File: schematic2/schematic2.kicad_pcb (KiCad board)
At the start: 2 copper layers, 68.8 x 56 mm, 52 parts, among them IC1 CAT24C32WI-GT3, J1 Barrel_Jack, K1 TIANBO_HJR_1-2C, P1 Conn_02x20_Odd_Even, Q1 BC547, Q2 BC557, Q3 BC547, Q4 BC547, U1 buck, U2 DS3231M, U3 MCP1700-1202E_SOT89

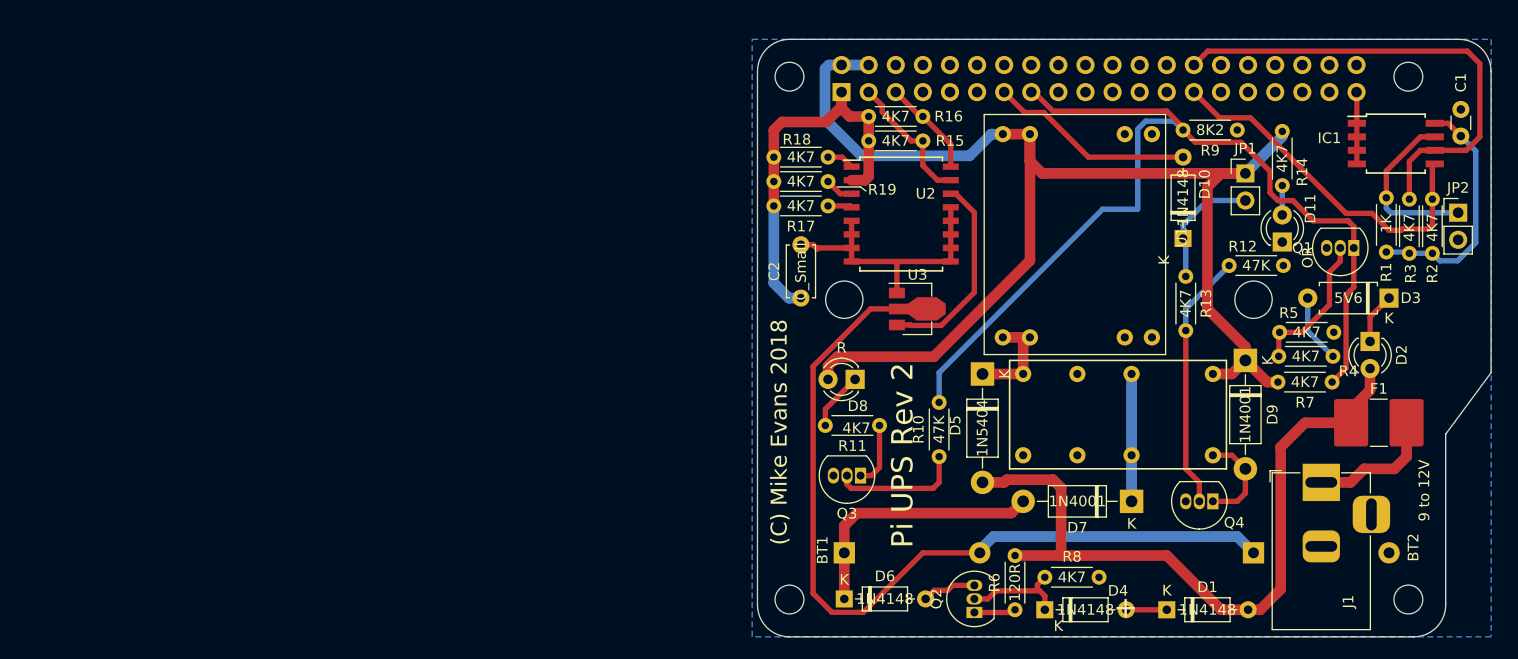
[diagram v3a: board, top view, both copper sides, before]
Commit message: Power the 3V line instead of the 5V.
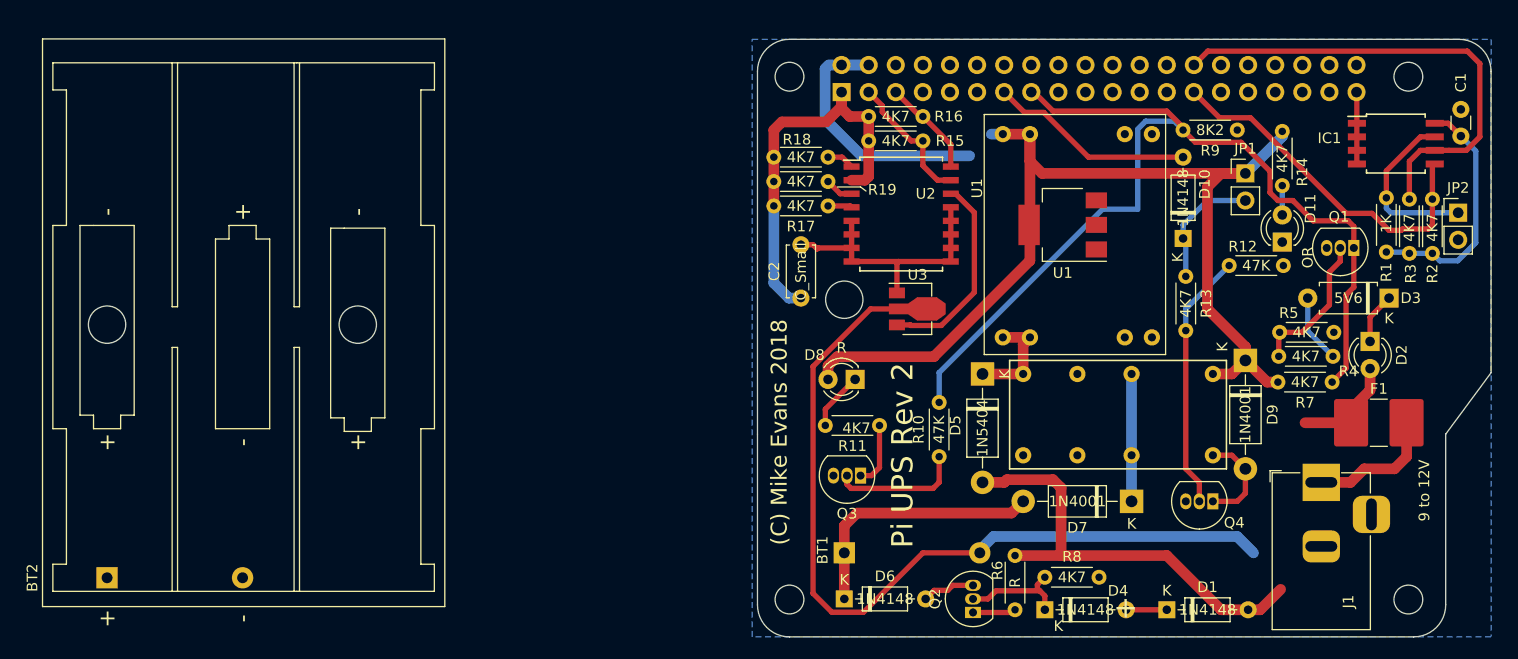
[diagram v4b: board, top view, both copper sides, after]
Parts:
- added U1: AP1117-33, Package_TO_SOT_SMD:SOT-223-3_TabPin2, F.Cu at (229.1, 111.4)
- BT2: value 3x AAA NiMh -> 4x AAA NiMh
- Q2: value BC557 -> 2N2907
- R6: value 120R -> R
- moved BT2 107.5 mm to (139.5, 144.5)
- moved Q2 0.13 mm to (220.7, 147.7)
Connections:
- BT1 pad 1: Net-(BT1-Pad1) -> (no net)
- D1 pad 2: +9V -> +5V
- D2 pad 2: +9V -> +5V
- D5 pad 1: Net-(D5-Pad1) -> Net-(C3-Pad1)
- D5 pad 2: +9V -> +5V
- D6 pad 1: Net-(BT1-Pad1) -> /Sheet5B4BA297/VI
- D7 pad 2: Net-(BT1-Pad1) -> /Sheet5B4BA297/VI
- D8 pad 2: +5V -> +3V3
- D9 pad 1: +5V -> Net-(C3-Pad1)
- F1 pad 1: +9V -> (no net)
- JP1 pad 1: +5V -> +3V3
- JP2 pad 2: Net-(JP2-Pad2) -> (no net)
- K1 pad 11: Net-(K1-Pad11) -> (no net)
- K1 pad 16: +5V -> Net-(C3-Pad1)
- K1 pad 6: Net-(K1-Pad6) -> (no net)
- K1 pad 8: Net-(K1-Pad8) -> (no net)
- K1 pad 9: Net-(D5-Pad1) -> Net-(C3-Pad1)
- P1 pad 10: /GPIO15(RXD0) -> (no net)
- P1 pad 11: /GPIO17(GEN0) -> (no net)
- P1 pad 12: /GPIO18(GEN1)(PWM0) -> (no net)
- P1 pad 16: /GPIO23(GEN4) -> (no net)
- P1 pad 17: Net-(P1-Pad17) -> (no net)
- P1 pad 18: /GPIO24(GEN5) -> (no net)
- P1 pad 19: /GPIO10(SPI0_MOSI) -> (no net)
- P1 pad 21: /GPIO9(SPI0_MISO) -> (no net)
- P1 pad 22: /GPIO25(GEN6) -> (no net)
- P1 pad 23: /GPIO11(SPI0_SCK) -> (no net)
- P1 pad 24: /GPIO8(SPI0_CE_N) -> (no net)
- P1 pad 26: /GPIO7(SPI1_CE_N) -> (no net)
- P1 pad 29: /GPIO5 -> (no net)
- P1 pad 3: SDA1 -> SCL1
- P1 pad 31: /GPIO6 -> (no net)
- P1 pad 32: /GPIO12(PWM0) -> (no net)
- P1 pad 33: /GPIO13(PWM1) -> (no net)
- P1 pad 35: /GPIO19(SPI1_MISO) -> (no net)
- P1 pad 36: /GPIO16 -> (no net)
- P1 pad 37: /GPIO26 -> (no net)
- P1 pad 38: /GPIO20(SPI1_MOSI) -> (no net)
- P1 pad 40: /GPIO21(SPI1_SCK) -> (no net)
- P1 pad 7: /GPIO4(GCLK) -> (no net)
- P1 pad 8: /GPIO14(TXD0) -> (no net)
- R14 pad 2: +5V -> +3V3
- R15 pad 1: SDA1 -> SCL1
- R2 pad 1: Net-(R2-Pad1) -> (no net)
- R3 pad 1: Net-(R3-Pad1) -> (no net)
- R6 pad 2: +9V -> +5V
- R7 pad 2: +5V -> +3V3
- U1 pad 4: +5V -> +3V3
- U2 pad 15: SDA1 -> SCL1
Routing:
- net +3V3: track 37.9 -> 134.9 mm
- net +9V: track 68.6 -> 0.00 mm
- net +5V: track 123.9 -> 76.0 mm
- net Net-(BT1-Pad1): track 24.6 -> 0.00 mm
- net /Sheet5B4BA297/VI: track 81.2 -> 105.8 mm
- net SDA1: track 12.9 -> 0.00 mm
- net SCL1: track 9.33 -> 22.2 mm

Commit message: Re-layout.
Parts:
- removed BT1: 3x AAA NiMh, Battery:BatteryHolder_Keystone_2479_3xAAA
- removed F1: Polyfuse, Fuse:Fuse_2816_7142Metric_Pad3.20x4.45mm_HandSolder
- removed IC1: CAT24C32WI-GT3, Package_SO:SOIJ-8_5.3x5.3mm_P1.27mm
- removed J1: Barrel_Jack, Connector_BarrelJack:BarrelJack_Horizontal
- removed MK1, MK2, MK3, MK4: M2.5, MountingHole:MountingHole_2.7mm_M2.5
- removed R3: 4K7, Resistor_THT:R_Axial_DIN0204_L3.6mm_D1.6mm_P5.08mm_Horizontal
- removed U3: MCP1700-1202E_SOT89, Package_TO_SOT_SMD:SOT-89-3
- added C3: 10uF, Capacitor_THT:CP_Radial_D6.3mm_P2.50mm, F.Cu at (214.7, 133.0)
- added C4: 22uF, Capacitor_THT:CP_Radial_D6.3mm_P2.50mm, F.Cu at (214.7, 125.4)
- added REF**: MountingHole_2.7mm_M2.5_Pad, MountingHole:MountingHole_2.7mm_M2.5_Pad, F.Cu at (203.4, 146.6)
- added REF**: MountingHole_2.7mm_M2.5_Pad, MountingHole:MountingHole_2.7mm_M2.5_Pad, F.Cu at (261.4, 146.6)
- added U4: CAT24C256, Package_SO:SOIC-8_3.9x4.9mm_P1.27mm, F.Cu at (261.0, 103.5)
- BT2: footprint Battery:BatteryHolder_Keystone_2479_3xAAA -> Connector_Molex:Molex_KK-254_AE-6410-02A_1x02_P2.54mm_Vertical
- C1: value 0.1uF -> C_Small
- C2: value C_Small -> 100nF
- R1: value 1K -> 4K7
- moved BT2 71.3 mm to (210.7, 139.8), turned to 180 degrees
- moved R11 43.6 mm to (254.9, 137.8), turned to 90 degrees
- moved D8 42.7 mm to (251.8, 132.5)
- moved Q3 40.2 mm to (250.3, 136.5), turned to 270 degrees
- moved R10 39.9 mm to (257.1, 137.8)
- moved R18 5.84 mm to (207.1, 110.9)
- moved R19 5.59 mm to (207.1, 112.9)
- moved U2 5.36 mm to (214.5, 115.7)
- moved R17 5.33 mm to (207.1, 114.9)
- moved R15 4.85 mm to (216.5, 108.3)
- moved R16 4.58 mm to (216.3, 105.8)
- moved R1 3.81 mm to (255.6, 108.9), turned to 90 degrees
- moved C2 2.34 mm to (202.8, 119.8), turned to 0 degrees
- moved U1 1.90 mm to (231.0, 111.1), turned to 90 degrees
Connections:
- BT2 pad 1: /Sheet5B4BA297/VI -> Net-(BT2-Pad1)
- C1 pad 1: +3.3V -> +3V3
- C2 pad 1: +3V3 -> /Sheet5B4BA297/VI
- D6 pad 1: /Sheet5B4BA297/VI -> Net-(BT2-Pad1)
- D7 pad 2: /Sheet5B4BA297/VI -> Net-(BT2-Pad1)
- D9 pad 2: Net-(D9-Pad2) -> /Sheet5B4BA297/VI
- JP2 pad 2: (no net) -> GND
- K1 pad 1: Net-(D9-Pad2) -> /Sheet5B4BA297/VI
- P1 pad 3: SCL1 -> SDA1
- Q4 pad 1: Net-(D9-Pad2) -> /Sheet5B4BA297/VI
- R1 pad 1: Net-(IC1-Pad7) -> +3V3
- R1 pad 2: +3.3V -> ID_SD
- R15 pad 2: +3V3 -> /Sheet5B4BA297/VI
- R16 pad 1: SCL1 -> SDA1
- R16 pad 2: +3V3 -> /Sheet5B4BA297/VI
- R17 pad 2: +3V3 -> /Sheet5B4BA297/VI
- R18 pad 2: +3V3 -> /Sheet5B4BA297/VI
- R19 pad 2: +3V3 -> /Sheet5B4BA297/VI
- R2 pad 1: (no net) -> +3V3
- R2 pad 2: ID_SD -> ID_SC
- U2 pad 14: Net-(U2-Pad14) -> (no net)
- U2 pad 15: SCL1 -> SDA1
- U2 pad 2: +3V3 -> /Sheet5B4BA297/VI
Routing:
- net Net-(C3-Pad1): track 0.00 -> 53.1 mm
- net +5V: track 76.0 -> 120.7 mm
- net POWER_FAIL: track 92.5 -> 65.0 mm
- net ID_SC: track 45.8 -> 70.3 mm, vias 0 -> 1
- net Net-(BT2-Pad1): track 0.00 -> 23.2 mm
- net +3.3V: track 22.9 -> 0.00 mm
- net SDA1: track 0.00 -> 20.3 mm
- net Net-(U2-Pad14): track 19.0 -> 0.00 mm
- net Net-(IC1-Pad7): track 16.3 -> 0.00 mm
- net +3V3: track 134.9 -> 148.8 mm
- net Net-(F1-Pad2): track 12.2 -> 0.00 mm
- net Net-(JP2-Pad1): track 0.00 -> 10.9 mm
- net Net-(D9-Pad2): track 9.22 -> 0.00 mm
- net /Sheet5B4BA297/VI: track 105.8 -> 97.7 mm
- net Net-(D5-Pad1): track 10.0 -> 2.54 mm
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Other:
- board text added: "(C) Mike Evans 2019"
- board text added: "A/V"
- board text added: "ACT"
- board text added: "BOTOM LEGEND"
- board text added: "BOTTOM ASSEMBLY"
- board text added: "C1"
- board text added: "C10"
- board text added: "C101"
- board text added: "C102"
- board text added: "C103"
- board text added: "C106"
- board text added: "C11"
- board text added: "C14"
- board text added: "C162"
- board text added: "C163"
- board text added: "C165"
- board text added: "C187"
- board text added: "C188"
- board text added: "C190"
- board text added: "C192"
- board text added: "C194"
- board text added: "C2"
- board text added: "C200"
- board text added: "C201"
- board text added: "C204"
- board text added: "C210"
- board text added: "C211"
- board text added: "C212"
- board text added: "C213"
- board text added: "C214"
- board text added: "C215"
- board text added: "C216"
- board text added: "C217"
- board text added: "C218"
- board text added: "C219"
- board text added: "C220"
- board text added: "C221"
- board text added: "C222"
- board text added: "C224"
- board text added: "C226"
- board text added: "C227"
- board text added: "C228"
- board text added: "C229"
- board text added: "C230"
- board text added: "C231"
- board text added: "C233"
- board text added: "C235"
- board text added: "C237"
- board text added: "C238"
- board text added: "C239"
- board text added: "C240"
- board text added: "C241"
- board text added: "C243"
- board text added: "C245"
- board text added: "C246"
- board text added: "C248"
- board text added: "C252"
- board text added: "C255"
- board text added: "C256"
- board text added: "C258"
- board text added: "C259"
- board text added: "C3"
- board text added: "C4"
- board text added: "C46"
- board text added: "C47"
- board text added: "C48"
- board text added: "C5"
- board text added: "C52"
- board text added: "C53"
- board text added: "C54"
- board text added: "C55"
- board text added: "C56"
- board text added: "C57"
- board text added: "C58"
- board text added: "C59"
- board text added: "C6"
- board text added: "C60"
- board text added: "C61"
- board text added: "C62"
- board text added: "C63"
- board text added: "C64"
- board text added: "C65"
- board text added: "C66"
- board text added: "C67"
- board text added: "C7"
- board text added: "C70"
- board text added: "C71"
- board text added: "C72"
- board text added: "C73"
- board text added: "C74"
- board text added: "C75"
- board text added: "C76"
- board text added: "C77"
- board text added: "C78"
- board text added: "C79"
- board text added: "C8"
- board text added: "C80"
- board text added: "C81"
- board text added: "C82"
- board text added: "C83"
- board text added: "C84"
- board text added: "C85"
- board text added: "C86"
- board text added: "C87"
- board text added: "C88"
- board text added: "C89"
- board text added: "C90"
- board text added: "C91"
- board text added: "C92"
- board text added: "C93"
- board text added: "C94"
- board text added: "C96"
- board text added: "C97"
- board text added: "C98"
- board text added: "C99"
- board text added: "CAMERA"
- board text added: "D3"
- board text added: "D4"
- board text added: "D5"
- board text added: "DISPLAY"
- board text added: "ETHERNET"
- board text added: "F1"
- board text added: "FB1"
- board text added: "FB2"
- board text added: "FB3"
- board text added: "FB4"
- board text added: "FB5"
- board text added: "FB6"
- board text added: "FB7"
- board text added: "FB8"
- board text added: "FCC ID: 2ABCB-RPI32"
- board text added: "GPIO"
- board text added: "HDMI"
- board text added: "IC: 20953-RPI32"
- board text added: "J1"
- board text added: "J10"
- board text added: "J11"
- board text added: "J12"
- board text added: "J13"
- board text added: "J3"
- board text added: "J4"
- board text added: "J5"
- board text added: "J6"
- board text added: "J7"
- board text added: "J8"
- board text added: "J9"
- board text added: "L1"
- board text added: "L2"
- board text added: "L3"
- board text added: "L4"
- board text added: "L5"
- board text added: "L6"
- board text added: "L7"
- board text added: "L8"
- board text added: "MICRO SD CARD"
- board text added: "Made in the UK"
- board text added: "PP1"
- board text added: "PP10"
- board text added: "PP11"
- board text added: "PP12"
- board text added: "PP13"
- board text added: "PP2"
- board text added: "PP20"
- board text added: "PP21"
- board text added: "PP22"
- board text added: "PP23"
- board text added: "PP24"
- board text added: "PP25"
- board text added: "PP26"
- board text added: "PP27"
- board text added: "PP28"
- board text added: "PP3"
- board text added: "PP35"
- board text added: "PP36"
- board text added: "PP39"
- board text added: "PP4"
- board text added: "PP40"
- board text added: "PP41"
- board text added: "PP42"
- board text added: "PP43"
- board text added: "PP44"
- board text added: "PP45"
- board text added: "PP46"
- board text added: "PP47"
- board text added: "PP48"
- board text added: "PP49"
- board text added: "PP5"
- board text added: "PP50"
- board text added: "PP51"
- board text added: "PP52"
- board text added: "PP53"
- board text added: "PP54"
- board text added: "PP55"
- board text added: "PP56"
- board text added: "PP57"
- board text added: "PP58"
- board text added: "PP59"
- board text added: "PP6"
- board text added: "PP60"
- board text added: "PP7"
- board text added: "PP8"
- board text added: "PP9"
- board text added: "PWR"
- board text added: "PWR IN"
- board text added: "Q1"
- board text added: "Q2"
- board text added: "Q3"
- board text added: "Q4"
- board text added: "Q5"
- board text added: "Q6"
- board text added: "Q7"
- board text added: "Q8"
- board text added: "R1"
- board text added: "R10"
- board text added: "R12"
- board text added: "R13"
- board text added: "R14"
- board text added: "R15"
- board text added: "R16"
- board text added: "R17"
- board text added: "R18"
- board text added: "R19"
- board text added: "R2"
- board text added: "R20"
- board text added: "R21"
- board text added: "R22"
- board text added: "R23"
- board text added: "R24"
- board text added: "R25"
- board text added: "R3"
- board text added: "R31"
- board text added: "R32"
- board text added: "R33"
- board text added: "R34"
- board text added: "R35"
- board text added: "R36"
- board text added: "R37"
- board text added: "R38"
- board text added: "R39"
- board text added: "R4"
- board text added: "R41"
- board text added: "R42"
- board text added: "R43"
- board text added: "R44"
- board text added: "R45"
- board text added: "R46"
- board text added: "R47"
- board text added: "R48"
- board text added: "R5"
- board text added: "R50"
- board text added: "R51"
- board text added: "R52"
- board text added: "R54"
- board text added: "R55"
- board text added: "R56"
- board text added: "R57"
- board text added: "R58"
- board text added: "R6"
- board text added: "R60"
- board text added: "R61"
- board text added: "R63"
- board text added: "R64"
- board text added: "R65"
- board text added: "R66"
- board text added: "R67"
- board text added: "R68"
- board text added: "R69"
- board text added: "R7"
- board text added: "R70"
- board text added: "R71"
- board text added: "R72"
- board text added: "R75"
- board text added: "R76"
- board text added: "R77"
- board text added: "R78"
- board text added: "R79"
- board text added: "R8"
- board text added: "R81"
- board text added: "R82"
- board text added: "R83"
- board text added: "RUN"
- board text added: "Raspberry Pi 3 Model B V1.2"
- board text added: "TOP ASSEMBLY"
- board text added: "TOP LEGEND"
- board text added: "U1"
- board text added: "U10"
- board text added: "U11"
- board text added: "U13"
- board text added: "U14"
- board text added: "U15"
- board text added: "U16"
- board text added: "U17"
- board text added: "U18"
- board text added: "U19"
- board text added: "U2"
- board text added: "U20"
- board text added: "U3"
- board text added: "U4"
- board text added: "U5"
- board text added: "U8"
- board text added: "U9"
- board text added: "X1"
- board text added: "X2"
- board text added: "c Raspberry Pi 2015"
- board text removed: "(C) Mike Evans 2018"
- board text removed: "9 to 12V"

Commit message: modified:   doc/UPS.adoc modified:   firmware/src/powermon.py modified:   schematic2/schematic2-cache.lib modified:   schematic2/schematic2.kicad_pcb modified:   schematic2/schematic2.sch
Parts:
- removed C3: 10uF, Capacitor_THT:CP_Radial_D6.3mm_P2.50mm
- removed C4: 22uF, Capacitor_THT:CP_Radial_D6.3mm_P2.50mm
- removed D7: 1N4001, Diode_THT:D_DO-41_SOD81_P10.16mm_Horizontal
- removed REF** (x2): MountingHole_2.7mm_M2.5_Pad, MountingHole:MountingHole_2.7mm_M2.5_Pad
- removed the U1 at (231.0, 111.1)
- removed the U1 at (231.8, 113.0)
- added H1: MountingHole, MountingHole:MountingHole_2.7mm, F.Cu at (203.4, 146.6)
- added H2: MountingHole, MountingHole:MountingHole_2.7mm, F.Cu at (261.3, 146.6)
- added R3: 4K7, Resistor_THT:R_Axial_DIN0204_L3.6mm_D1.6mm_P5.08mm_Horizontal, F.Cu at (237.4, 108.5)
- added RV1: R_POT_TRIM, Potentiometer_THT:Potentiometer_Runtron_RM-065_Vertical, F.Cu at (231.9, 111.6)
- added U1: AP1117-33, Package_TO_SOT_SMD:SOT-223-3_TabPin2, F.Cu at (214.9, 127.3)
- D3: value 5V6 -> 3V0
- D5: value 1N5404 -> BAT86; footprint Diode_THT:D_DO-41_SOD81_P10.16mm_Horizontal -> Diode_THT:D_DO-35_SOD27_P7.62mm_Horizontal
- D6: value 1N4148 -> BAT86
- R9: value 8K2 -> 4K7
- moved Q1 34.4 mm to (223.6, 103.0), turned to 270 degrees
- moved R5 28.0 mm to (224.5, 108.7), turned to 270 degrees
- moved D6 25.2 mm to (232.3, 137.7), turned to 180 degrees
- moved D3 25.1 mm to (234.6, 117.0)
- moved R4 22.2 mm to (234.6, 113.7), turned to 90 degrees
- moved D2 21.6 mm to (236.5, 120.1)
- moved D5 17.0 mm to (214.3, 140.7), turned to 0 degrees
- moved R1 11.2 mm to (266.5, 111.6), turned to 180 degrees
- moved R9 8.15 mm to (237.4, 101.1), turned to 270 degrees
- moved JP2 8.12 mm to (258.3, 108.2), turned to 270 degrees
- moved R2 6.72 mm to (266.6, 108.0), turned to 180 degrees
- moved K1 1.35 mm to (242.2, 133.9)
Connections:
- C2 pad 1: /Sheet5B4BA297/VI -> +3V3
- D10 pad 1: Net-(D10-Pad1) -> +5V
- D5 pad 1: Net-(C3-Pad1) -> Net-(BT2-Pad1)
- D5 pad 2: +5V -> Net-(D5-Pad2)
- D6 pad 1: Net-(BT2-Pad1) -> Net-(D6-Pad1)
- D6 pad 2: Net-(D6-Pad2) -> Net-(BT2-Pad1)
- D8 pad 2: +3V3 -> +5V
- D9 pad 1: Net-(C3-Pad1) -> +5V
- D9 pad 2: /Sheet5B4BA297/VI -> Net-(D9-Pad2)
- JP1 pad 1: +3V3 -> +5V
- JP1 pad 2: Net-(D10-Pad1) -> (no net)
- K1 pad 1: /Sheet5B4BA297/VI -> Net-(D9-Pad2)
- K1 pad 13: Net-(D7-Pad1) -> Net-(D6-Pad1)
- K1 pad 16: Net-(C3-Pad1) -> +5V
- K1 pad 4: Net-(D7-Pad1) -> Net-(D6-Pad1)
- K1 pad 8: (no net) -> +5V
- K1 pad 9: Net-(C3-Pad1) -> +5V
- Q2 pad 3: Net-(D6-Pad2) -> Net-(D5-Pad2)
- Q4 pad 1: /Sheet5B4BA297/VI -> Net-(D9-Pad2)
- R13 pad 1: Net-(D10-Pad1) -> +5V
- R14 pad 2: +3V3 -> +5V
- R15 pad 2: /Sheet5B4BA297/VI -> +3V3
- R16 pad 2: /Sheet5B4BA297/VI -> +3V3
- R17 pad 2: /Sheet5B4BA297/VI -> +3V3
- R18 pad 2: /Sheet5B4BA297/VI -> +3V3
- R19 pad 2: /Sheet5B4BA297/VI -> +3V3
- R4 pad 2: Net-(Q1-Pad2) -> Net-(R4-Pad2)
- R5 pad 1: Net-(Q1-Pad2) -> Net-(R5-Pad1)
- R7 pad 2: +3V3 -> +5V
- R9 pad 2: POWER_FAIL -> Net-(R3-Pad1)
- U2 pad 14: (no net) -> V_BAT
- U2 pad 2: /Sheet5B4BA297/VI -> +3V3
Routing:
- net /Sheet5B4BA297/VI: track 97.7 -> 0.00 mm
- net Net-(C3-Pad1): track 53.1 -> 0.00 mm
- net +5V: track 120.7 -> 164.6 mm, vias 0 -> 1
- net ID_SC: track 70.3 -> 36.5 mm, vias 1 -> 0
- net +3V3: track 148.8 -> 124.2 mm
- net V_BAT: track 0.00 -> 24.2 mm
- net Net-(D6-Pad1): track 0.00 -> 13.1 mm
- net Net-(D7-Pad1): track 11.9 -> 0.00 mm
- net Net-(D10-Pad1): track 11.4 -> 0.00 mm
- net Net-(D9-Pad2): track 0.00 -> 8.07 mm
- net Net-(Q1-Pad2): track 14.2 -> 6.75 mm
- net Net-(BT2-Pad1): track 23.2 -> 16.4 mm
- net Net-(D5-Pad2): track 0.00 -> 4.99 mm
- net Net-(D6-Pad2): track 4.97 -> 0.00 mm
- net Net-(R4-Pad2): track 0.00 -> 3.67 mm
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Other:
- board size 68.8 x 56 mm -> 68.4 x 56 mm
- board text removed: "BOTOM LEGEND"
- board text removed: "BOTTOM ASSEMBLY"
- board text removed: "TOP ASSEMBLY"
- board text removed: "TOP LEGEND"

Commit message: Mostly layout changes.
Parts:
- removed JP1: UPS, Connector_PinHeader_2.54mm:PinHeader_1x02_P2.54mm_Vertical
- removed JP2: Jumper_NO_Small, Connector_PinHeader_2.54mm:PinHeader_1x02_P2.54mm_Vertical
- removed the R1 at (266.5, 111.6)
- removed the R10 at (257.1, 137.8)
- removed R16, R17, R18, R19: 4K7, Resistor_THT:R_Axial_DIN0204_L3.6mm_D1.6mm_P5.08mm_Horizontal
- removed the R2 at (266.6, 108.0)
- removed the R6 at (224.6, 147.5)
- removed the R8 at (227.4, 144.4)
- removed RV1: R_POT_TRIM, Potentiometer_THT:Potentiometer_Runtron_RM-065_Vertical
- removed U4: CAT24C256, Package_SO:SOIC-8_3.9x4.9mm_P1.27mm
- added BT1: Battery_Cell, Connector_Molex:Molex_KK-254_AE-6410-02A_1x02_P2.54mm_Vertical, F.Cu at (211.0, 123.0)
- added C3: 100n, Capacitor_SMD:C_0805_2012Metric, F.Cu at (205.5, 123.9)
- added D12: 3V6, Resistor_THT:R_Axial_DIN0207_L6.3mm_D2.5mm_P7.62mm_Horizontal, F.Cu at (209.5, 136.9)
- added D13: 1N4001, Diode_SMD:D_2010_5025Metric, F.Cu at (215.2, 144.5)
- added D14: 1N4001, Diode_SMD:D_2010_5025Metric, F.Cu at (246.5, 143.8)
- added D15: 1N4001, Diode_SMD:D_2010_5025Metric, F.Cu at (204.0, 114.7)
- added D7: 1N4001, Diode_SMD:D_2010_5025Metric, F.Cu at (214.8, 133.0)
- added F1: Polyfuse, Fuse:Fuse_2816_7142Metric_Pad3.20x4.45mm_HandSolder, F.Cu at (260.5, 130.4)
- added H3: MountingHole, MountingHole:MountingHole_3.2mm_M3, F.Cu at (261.3, 146.4)
- added H5: MountingHole, MountingHole:MountingHole_3.2mm_M3, F.Cu at (261.5, 97.5)
- added J1: Barrel_Jack, Connector_BarrelJack:BarrelJack_Horizontal, F.Cu at (253.3, 135.5)
- added Q5: BC547, Package_TO_SOT_THT:TO-92L_Inline_Wide, F.Cu at (225.5, 147.0)
- added R12: 4K7, Resistor_THT:R_Axial_DIN0204_L3.6mm_D1.6mm_P5.08mm_Horizontal, F.Cu at (220.0, 102.0)
- added R13: 4K7, Resistor_THT:R_Axial_DIN0204_L3.6mm_D1.6mm_P5.08mm_Horizontal, F.Cu at (208.5, 102.0)
- added R14: 2K2, Resistor_THT:R_Axial_DIN0204_L3.6mm_D1.6mm_P5.08mm_Horizontal, F.Cu at (221.0, 129.5)
- added R5: 470R, Resistor_THT:R_Axial_DIN0204_L3.6mm_D1.6mm_P5.08mm_Horizontal, F.Cu at (221.0, 147.0)
- added R7: 47K, Resistor_THT:R_Axial_DIN0204_L3.6mm_D1.6mm_P5.08mm_Horizontal, F.Cu at (259.9, 110.2)
- added U3: LM317_SOT-223, Package_TO_SOT_THT:TO-92L_Inline_Wide, F.Cu at (234.0, 146.0)
- BT2: value 4x AAA NiMh -> Battery_Cell
- C1: value C_Small -> 100n; footprint Capacitor_THT:C_Disc_D3.0mm_W1.6mm_P2.50mm -> Capacitor_THT:C_Disc_D4.3mm_W1.9mm_P5.00mm
- C2: footprint Capacitor_THT:C_Disc_D4.7mm_W2.5mm_P5.00mm -> Capacitor_SMD:C_0805_2012Metric
- D1: value 1N4148 -> LED; footprint Diode_THT:D_DO-35_SOD27_P7.62mm_Horizontal -> LED_THT:LED_D3.0mm
- D10: footprint Diode_THT:D_DO-35_SOD27_P7.62mm_Horizontal -> Diode_SMD:D_2010_5025Metric
- D3: value 3V0 -> 5V6
- D4: value 1N4148 -> 3V6; footprint Diode_THT:D_DO-35_SOD27_P7.62mm_Horizontal -> Resistor_THT:R_Axial_DIN0207_L6.3mm_D2.5mm_P7.62mm_Horizontal
- D5, D6: value BAT86 -> 1N4001; footprint Diode_THT:D_DO-35_SOD27_P7.62mm_Horizontal -> Diode_SMD:D_2010_5025Metric
- D9: footprint Diode_THT:D_DO-41_SOD81_P10.16mm_Horizontal -> Diode_SMD:D_2010_5025Metric
- H1, H2: footprint MountingHole:MountingHole_2.7mm -> MountingHole:MountingHole_3.2mm_M3
- Q2: value 2N2907 -> DMP1045U; footprint Package_TO_SOT_THT:TO-92_Inline -> Package_TO_SOT_SMD:SOT-23
- R11: renamed from R14; value 4K7 -> 1K
- R15: value 4K7 -> 320R
- R3: value 4K7 -> 6R6; footprint Resistor_THT:R_Axial_DIN0204_L3.6mm_D1.6mm_P5.08mm_Horizontal -> Resistor_THT:R_Axial_DIN0207_L6.3mm_D2.5mm_P7.62mm_Horizontal
- R6: renamed from R9; value 4K7 -> 8K2
- U1: value AP1117-33 -> buck; footprint Package_TO_SOT_SMD:SOT-223-3_TabPin2 -> Mikee:BUCK_MODULE_5V
- moved H2 57.8 mm to (203.6, 146.4)
- moved C1 50.9 mm to (242.5, 148.0)
- moved H1 49.1 mm to (203.4, 97.5)
- moved R3 39.4 mm to (204.0, 129.4)
- moved Q1 34.4 mm to (255.9, 114.9), turned to 90 degrees
- moved Q4 33.1 mm to (254.8, 106.3)
- moved Q3 33.1 mm to (259.0, 104.6), turned to 0 degrees
- moved D8 30.8 mm to (266.1, 105.1), turned to 90 degrees
- moved R8 30.5 mm to (259.1, 107.6), turned to 0 degrees
- moved D2 29.6 mm to (266.0, 122.3)
- moved R2 28.0 mm to (249.4, 121.5), turned to 0 degrees
- moved D3 25.1 mm to (259.7, 118.2)
- moved U1 24.1 mm to (236.1, 115.8), turned to 90 degrees
- moved D4 23.5 mm to (217.5, 126.1), turned to 90 degrees
- moved BT2 22.8 mm to (211.0, 117.0), turned to 270 degrees
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- renumbered R4 to R1, R13 to R10, R5 to R2, R7 to R4, R11 to R8, R12 to R9
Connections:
- BT2 pad 1: Net-(BT2-Pad1) -> CLK_BAT
- BT2 pad 2: GND -> Net-(BT2-Pad2)
- C1 pad 1: +3V3 -> Net-(C1-Pad1)
- D1 pad 2: +5V -> Net-(D1-Pad2)
- D10 pad 1: +5V -> Net-(D10-Pad1)
- D11 pad 1: GND -> Net-(D11-Pad1)
- D2 pad 2: +5V -> +9V
- D4 pad 1: Net-(D4-Pad1) -> Net-(BT1-Pad1)
- D4 pad 2: Net-(D1-Pad1) -> Net-(D4-Pad2)
- D5 pad 1: Net-(BT2-Pad1) -> Net-(D5-Pad1)
- D5 pad 2: Net-(D5-Pad2) -> +9V
- D6 pad 1: Net-(D6-Pad1) -> CLK_BAT
- D6 pad 2: Net-(BT2-Pad1) -> Net-(D4-Pad2)
- D9 pad 2: Net-(D9-Pad2) -> Net-(D11-Pad1)
- K1 pad 1: Net-(D9-Pad2) -> Net-(D11-Pad1)
- K1 pad 13: Net-(D6-Pad1) -> Net-(K1-Pad13)
- K1 pad 4: Net-(D6-Pad1) -> (no net)
- K1 pad 8: +5V -> (no net)
- K1 pad 9: +5V -> Net-(D5-Pad1)
- P1 pad 27: ID_SD -> (no net)
- P1 pad 28: ID_SC -> (no net)
- Q2 pad 1: Net-(Q2-Pad1) -> +9V
- Q2 pad 2: Net-(D4-Pad1) -> Net-(D7-Pad1)
- Q2 pad 3: Net-(D5-Pad2) -> Net-(K1-Pad13)
- Q4 pad 1: Net-(D9-Pad2) -> Net-(D11-Pad1)
- R1 pad 2: Net-(R4-Pad2) -> Net-(Q1-Pad2)
- R10 pad 1: +5V -> Net-(D10-Pad1)
- R15 pad 1: SCL1 -> Net-(R14-Pad2)
- R15 pad 2: +3V3 -> Net-(BT2-Pad2)
- R2 pad 1: Net-(R5-Pad1) -> Net-(Q1-Pad2)
- R3 pad 1: Net-(R3-Pad1) -> Net-(BT2-Pad2)
- R3 pad 2: POWER_FAIL -> GND
- R6 pad 2: Net-(R3-Pad1) -> POWER_FAIL
- U1 pad 1: GND -> Net-(D5-Pad1)
- U1 pad 2: V_BAT -> GND
- U1 pad 3: +5V -> GND
- U2 pad 1: Net-(R18-Pad1) -> (no net)
- U2 pad 14: V_BAT -> CLK_BAT
- U2 pad 3: Net-(R19-Pad1) -> (no net)
- U2 pad 4: Net-(R17-Pad1) -> (no net)
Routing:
- net +3V3: track 124.2 -> 28.2 mm
- net +9V: track 0.00 -> 87.4 mm
- net Net-(BT1-Pad1): track 0.00 -> 74.6 mm
- net Net-(BT2-Pad2): track 0.00 -> 66.5 mm
- net Net-(D11-Pad1): track 0.00 -> 59.3 mm
- net CLK_BAT: track 0.00 -> 48.1 mm
- net +5V: track 164.6 -> 122.1 mm, vias 1 -> 0
- net ID_SD: track 37.1 -> 0.00 mm
- net ID_SC: track 36.5 -> 0.00 mm
- net Net-(D1-Pad2): track 0.00 -> 30.7 mm
- net V_BAT: track 24.2 -> 0.00 mm
- net GND: track 38.5 -> 59.2 mm
- net Net-(K1-Pad13): track 0.00 -> 19.8 mm
- net Net-(BT2-Pad1): track 16.4 -> 0.00 mm
- net Net-(Q4-Pad2): track 27.6 -> 12.2 mm
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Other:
- board size 68.4 x 56 mm -> 68.8 x 56 mm
- net class Bat_Charge added: clearance 0.1, trace_width 0.25, via_dia 0.9, via_drill 0.6
- board text added: "(C) Mike Evans 2020"
- board text added: "12V"
- board text removed: "(C) Mike Evans 2019"
- board text removed: "A/V"
- board text removed: "ACT"
- board text removed: "C1"
- board text removed: "C10"
- board text removed: "C101"
- board text removed: "C102"
- board text removed: "C103"
- board text removed: "C106"
- board text removed: "C11"
- board text removed: "C14"
- board text removed: "C162"
- board text removed: "C163"
- board text removed: "C165"
- board text removed: "C187"
- board text removed: "C188"
- board text removed: "C190"
- board text removed: "C192"
- board text removed: "C194"
- board text removed: "C2"
- board text removed: "C200"
- board text removed: "C201"
- board text removed: "C204"
- board text removed: "C210"
- board text removed: "C211"
- board text removed: "C212"
- board text removed: "C213"
- board text removed: "C214"
- board text removed: "C215"
- board text removed: "C216"
- board text removed: "C217"
- board text removed: "C218"
- board text removed: "C219"
- board text removed: "C220"
- board text removed: "C221"
- board text removed: "C222"
- board text removed: "C224"
- board text removed: "C226"
- board text removed: "C227"
- board text removed: "C228"
- board text removed: "C229"
- board text removed: "C230"
- board text removed: "C231"
- board text removed: "C233"
- board text removed: "C235"
- board text removed: "C237"
- board text removed: "C238"
- board text removed: "C239"
- board text removed: "C240"
- board text removed: "C241"
- board text removed: "C243"
- board text removed: "C245"
- board text removed: "C246"
- board text removed: "C248"
- board text removed: "C252"
- board text removed: "C255"
- board text removed: "C256"
- board text removed: "C258"
- board text removed: "C259"
- board text removed: "C3"
- board text removed: "C4"
- board text removed: "C46"
- board text removed: "C47"
- board text removed: "C48"
- board text removed: "C5"
- board text removed: "C52"
- board text removed: "C53"
- board text removed: "C54"
- board text removed: "C55"
- board text removed: "C56"
- board text removed: "C57"
- board text removed: "C58"
- board text removed: "C59"
- board text removed: "C6"
- board text removed: "C60"
- board text removed: "C61"
- board text removed: "C62"
- board text removed: "C63"
- board text removed: "C64"
- board text removed: "C65"
- board text removed: "C66"
- board text removed: "C67"
- board text removed: "C7"
- board text removed: "C70"
- board text removed: "C71"
- board text removed: "C72"
- board text removed: "C73"
- board text removed: "C74"
- board text removed: "C75"
- board text removed: "C76"
- board text removed: "C77"
- board text removed: "C78"
- board text removed: "C79"
- board text removed: "C8"
- board text removed: "C80"
- board text removed: "C81"
- board text removed: "C82"
- board text removed: "C83"
- board text removed: "C84"
- board text removed: "C85"
- board text removed: "C86"
- board text removed: "C87"
- board text removed: "C88"
- board text removed: "C89"
- board text removed: "C90"
- board text removed: "C91"
- board text removed: "C92"
- board text removed: "C93"
- board text removed: "C94"
- board text removed: "C96"
- board text removed: "C97"
- board text removed: "C98"
- board text removed: "C99"
- board text removed: "CAMERA"
- board text removed: "D3"
- board text removed: "D4"
- board text removed: "D5"
- board text removed: "DISPLAY"
- board text removed: "ETHERNET"
- board text removed: "F1"
- board text removed: "FB1"
- board text removed: "FB2"
- board text removed: "FB3"
- board text removed: "FB4"
- board text removed: "FB5"
- board text removed: "FB6"
- board text removed: "FB7"
- board text removed: "FB8"
- board text removed: "FCC ID: 2ABCB-RPI32"
- board text removed: "GPIO"
- board text removed: "HDMI"
- board text removed: "IC: 20953-RPI32"
- board text removed: "J1"
- board text removed: "J10"
- board text removed: "J11"
- board text removed: "J12"
- board text removed: "J13"
- board text removed: "J3"
- board text removed: "J4"
- board text removed: "J5"
- board text removed: "J6"
- board text removed: "J7"
- board text removed: "J8"
- board text removed: "J9"
- board text removed: "L1"
- board text removed: "L2"
- board text removed: "L3"
- board text removed: "L4"
- board text removed: "L5"
- board text removed: "L6"
- board text removed: "L7"
- board text removed: "L8"
- board text removed: "MICRO SD CARD"
- board text removed: "Made in the UK"
- board text removed: "PP1"
- board text removed: "PP10"
- board text removed: "PP11"
- board text removed: "PP12"
- board text removed: "PP13"
- board text removed: "PP2"
- board text removed: "PP20"
- board text removed: "PP21"
- board text removed: "PP22"
- board text removed: "PP23"
- board text removed: "PP24"
- board text removed: "PP25"
- board text removed: "PP26"
- board text removed: "PP27"
- board text removed: "PP28"
- board text removed: "PP3"
- board text removed: "PP35"
- board text removed: "PP36"
- board text removed: "PP39"
- board text removed: "PP4"
- board text removed: "PP40"
- board text removed: "PP41"
- board text removed: "PP42"
- board text removed: "PP43"
- board text removed: "PP44"
- board text removed: "PP45"
- board text removed: "PP46"
- board text removed: "PP47"
- board text removed: "PP48"
- board text removed: "PP49"
- board text removed: "PP5"
- board text removed: "PP50"
- board text removed: "PP51"
- board text removed: "PP52"
- board text removed: "PP53"
- board text removed: "PP54"
- board text removed: "PP55"
- board text removed: "PP56"
- board text removed: "PP57"
- board text removed: "PP58"
- board text removed: "PP59"
- board text removed: "PP6"
- board text removed: "PP60"
- board text removed: "PP7"
- board text removed: "PP8"
- board text removed: "PP9"
- board text removed: "PWR"
- board text removed: "PWR IN"
- board text removed: "Q1"
- board text removed: "Q2"
- board text removed: "Q3"
- board text removed: "Q4"
- board text removed: "Q5"
- board text removed: "Q6"
- board text removed: "Q7"
- board text removed: "Q8"
- board text removed: "R1"
- board text removed: "R10"
- board text removed: "R12"
- board text removed: "R13"
- board text removed: "R14"
- board text removed: "R15"
- board text removed: "R16"
- board text removed: "R17"
- board text removed: "R18"
- board text removed: "R19"
- board text removed: "R2"
- board text removed: "R20"
- board text removed: "R21"
- board text removed: "R22"
- board text removed: "R23"
- board text removed: "R24"
- board text removed: "R25"
- board text removed: "R3"
- board text removed: "R31"
- board text removed: "R32"
- board text removed: "R33"
- board text removed: "R34"
- board text removed: "R35"
- board text removed: "R36"
- board text removed: "R37"
- board text removed: "R38"
- board text removed: "R39"
- board text removed: "R4"
- board text removed: "R41"
- board text removed: "R42"
- board text removed: "R43"
- board text removed: "R44"
- board text removed: "R45"
- board text removed: "R46"
- board text removed: "R47"
- board text removed: "R48"
- board text removed: "R5"
- board text removed: "R50"
- board text removed: "R51"
- board text removed: "R52"
- board text removed: "R54"
- board text removed: "R55"
- board text removed: "R56"
- board text removed: "R57"
- board text removed: "R58"
- board text removed: "R6"
- board text removed: "R60"
- board text removed: "R61"
- board text removed: "R63"
- board text removed: "R64"
- board text removed: "R65"
- board text removed: "R66"
- board text removed: "R67"
- board text removed: "R68"
- board text removed: "R69"
- board text removed: "R7"
- board text removed: "R70"
- board text removed: "R71"
- board text removed: "R72"
- board text removed: "R75"
- board text removed: "R76"
- board text removed: "R77"
- board text removed: "R78"
- board text removed: "R79"
- board text removed: "R8"
- board text removed: "R81"
- board text removed: "R82"
- board text removed: "R83"
- board text removed: "RUN"
- board text removed: "Raspberry Pi 3 Model B V1.2"
- board text removed: "U1"
- board text removed: "U10"
- board text removed: "U11"
- board text removed: "U13"
- board text removed: "U14"
- board text removed: "U15"
- board text removed: "U16"
- board text removed: "U17"
- board text removed: "U18"
- board text removed: "U19"
- board text removed: "U2"
- board text removed: "U20"
- board text removed: "U3"
- board text removed: "U4"
- board text removed: "U5"
- board text removed: "U8"
- board text removed: "U9"
- board text removed: "X1"
- board text removed: "X2"
- board text removed: "c Raspberry Pi 2015"
